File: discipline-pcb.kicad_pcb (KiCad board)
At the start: 2 copper layers, 304.9 x 122.8 mm, 180 parts, among them J1 AVR-ISP-6, SW1 KEYSW, SW10 KEYSW, SW11 KEYSW, SW12 KEYSW, SW13 KEYSW, SW14 KEYSW, SW15 KEYSW, SW16 KEYSW, SW17 KEYSW, SW18 KEYSW, SW19 KEYSW, SW2 KEYSW, SW20 KEYSW, SW21 KEYSW, SW22 KEYSW, SW23 KEYSW, SW24 KEYSW, SW25 KEYSW, SW26 KEYSW, SW27 KEYSW, SW28 KEYSW, SW29 KEYSW, SW3 KEYSW, SW30 KEYSW, SW31 KEYSW, SW32 KEYSW, SW33 KEYSW, SW34 KEYSW, SW35 KEYSW, SW36 KEYSW, SW37 KEYSW, SW38 KEYSW, SW39 KEYSW, SW4 KEYSW, SW40 KEYSW, SW41 KEYSW, SW42 KEYSW, SW43 KEYSW, SW44 KEYSW, SW45 KEYSW, SW46 KEYSW, SW47 KEYSW, SW48 KEYSW, SW49 KEYSW, SW5 KEYSW, SW50 KEYSW, SW51 KEYSW, SW52 KEYSW, SW53 KEYSW, SW54 KEYSW, SW55 KEYSW, SW56 KEYSW, SW57 KEYSW, SW58 KEYSW, SW59 KEYSW, SW6 KEYSW, SW60 KEYSW, SW61 KEYSW, SW62 KEYSW, SW63 KEYSW, SW64 KEYSW, SW65 KEYSW, SW66 KEYSW, SW67 KEYSW, SW68 KEYSW, SW7 KEYSW, SW8 KEYSW, SW9 KEYSW, U1 ATmega32A-PU, Y1 Crystal

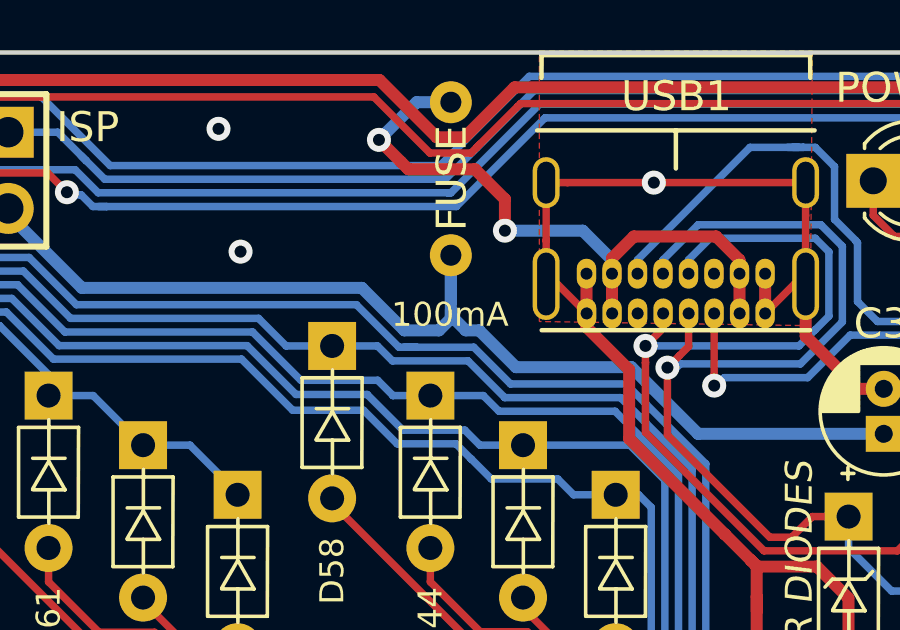
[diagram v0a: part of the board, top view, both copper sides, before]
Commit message: change fuse value
change fuse value from 100mA to 500mA. 100mA is fine for this use, but 500mA is USB 2.0 standard
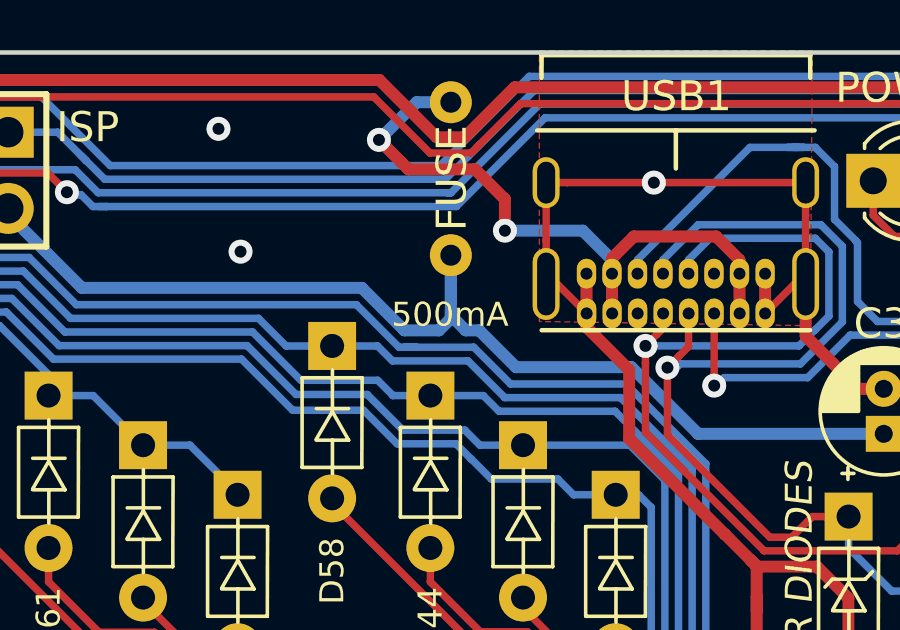
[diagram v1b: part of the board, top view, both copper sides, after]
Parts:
- F1: value 100mA -> 500mA
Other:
- board text added: "500mA"
- board text removed: "100mA"
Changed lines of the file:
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@@
       (effects (font (size 1 1) (thickness 0.15)))
     )
-    (fp_text value 100mA (at 0 -1.905 90) (layer F.Fab)
+    (fp_text value 500mA (at 0 -1.905 90) (layer F.Fab)
       (effects (font (size 1 1) (thickness 0.15)))
     )
@@
       (xy -5.108836 -0.98406)) (layer F.Cu) (width 0.01))
   )
-  (gr_text 100mA (at 276.795589 61.679275) (layer F.SilkS)
+  (gr_text 500mA (at 276.795589 61.679275) (layer F.SilkS)
     (effects (font (size 0.8 0.8) (thickness 0.1)))
   )

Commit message: Update discipline-pcb.kicad_pcb
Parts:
- removed ST62: 6.25U, MX_Alps_Hybrid:MX-6.25U-Stabilizer
- removed the SW31 at (75.0, 123.0)
- removed the SW59 at (77.4, 161.1)
- removed the SW61 at (106.0, 161.1)
- removed the SW62 at (187.0, 161.1)
- removed the SW63 at (268.0, 161.1)
- removed the SW64 at (296.5, 161.1)
- added REF**: 6.25U, cftkb:MX-6.25U-Stabilizer, F.Cu at (191.6, 166.2)
- added SW69: KEYSW, cftkb:SW_Cherry_MX1A_1.25u_PCBNOSCREEN, F.Cu at (75.0, 123.0)
- added SW70: KEYSW, cftkb:SW_Cherry_MX1A_1.50u_PCBNOSCREEN, F.Cu at (77.4, 161.1)
- added SW71: KEYSW, cftkb:SW_Cherry_MX1A_1.50u_PCBNOSCREEN, F.Cu at (106.0, 161.1)
- added SW72: KEYSW, cftkb:SW_Cherry_MX1A_1.00u_PCB-NOSCREEN, F.Cu at (187.0, 161.1)
- added SW73: KEYSW, cftkb:SW_Cherry_MX1A_1.50u_PCBNOSCREEN, F.Cu at (268.0, 161.1)
- added SW74: KEYSW, cftkb:SW_Cherry_MX1A_1.50u_PCBNOSCREEN, F.Cu at (296.5, 161.1)
- BOOT1, RESET1: footprint Button_Switch_THT:SW_PUSH_6mm -> cftkb:SW_PUSH_6mm
- C1, C2: footprint Capacitor_THT:C_Disc_D3.0mm_W1.6mm_P2.50mm -> cftkb:C_Disc_D3.0mm_W1.6mm_P2.50mm
- C3: footprint Capacitor_THT:CP_Radial_D4.0mm_P1.50mm -> cftkb:CP_Radial_D4.0mm_P1.50mm
- C4, C5: footprint Capacitor_THT:C_Disc_D4.3mm_W1.9mm_P5.00mm -> cftkb:C_Disc_D4.3mm_W1.9mm_P5.00mm
- D1, D10, D11, D12, D13, D14, D15, D16, D17, D18, D19, D2, D20, D21, D22, D23, D24, D25, D26, D27, D28, D29, D3, D30, D31, D32, D33, D34, D35, D36, D37, D38, D39, D4, D40, D41, D42, D43, D44, D45, D46, D47, D48, D49, D5, D50, D51, D52, D53, D54, D55, D56, D57, D58, D59, D6, D60, D61, D62, D63, D64, D65, D66, D67, D68, D7, D8, D9: footprint Diode_THT:D_DO-35_SOD27_P5.08mm_Horizontal -> cftkb:D_DO-35_SOD27_P5.08mm_Horizontal
- D69, D70: value 3V6 -> 3.6V; footprint Diode_THT:D_DO-35_SOD27_P5.08mm_Horizontal -> cftkb:D_DO-35_SOD27_P5.08mm_Horizontal
- F1: footprint keyboard_parts:polyfuse_5.1mm -> cftkb:polyfuse_5.1mm
- J1: footprint keyboard_parts:AVR_ICSP_3x2 -> cftkb:AVR_ICSP_3x2
- LED1: footprint LED_THT:LED_D3.0mm -> cftkb:LED_D3.0mm
- R1, R2, R3, R4, R6: footprint Resistor_THT:R_Axial_DIN0204_L3.6mm_D1.6mm_P7.62mm_Horizontal -> cftkb:R_Axial_DIN0204_L3.6mm_D1.6mm_P7.62mm_Horizontal
- R5: value 1.5K -> 1.5k; footprint Resistor_THT:R_Axial_DIN0204_L3.6mm_D1.6mm_P7.62mm_Horizontal -> cftkb:R_Axial_DIN0204_L3.6mm_D1.6mm_P7.62mm_Horizontal
- R7: value 10K -> 10k; footprint Resistor_THT:R_Axial_DIN0204_L3.6mm_D1.6mm_P7.62mm_Horizontal -> cftkb:R_Axial_DIN0204_L3.6mm_D1.6mm_P7.62mm_Horizontal
- ST72: renamed from ST62; footprint MX_Alps_Hybrid:MX-7U-Stabilizer -> cftkb:MX-7U-Stabilizer
- SW1, SW10, SW11, SW12, SW13, SW15, SW17, SW18, SW19, SW2, SW20, SW21, SW22, SW23, SW24, SW25, SW26, SW27, SW28, SW3, SW30, SW32, SW33, SW34, SW35, SW36, SW37, SW38, SW39, SW4, SW40, SW41, SW42, SW44, SW46, SW47, SW48, SW49, SW5, SW50, SW51, SW52, SW53, SW54, SW55, SW57, SW58, SW6, SW62, SW63, SW64, SW65, SW66, SW67, SW68, SW7, SW8, SW9: footprint Button_Switch_Keyboard:SW_Cherry_MX1A_1.00u_PCB-NOSCREEN -> cftkb:SW_Cherry_MX1A_1.00u_PCB-NOSCREEN
- SW14: footprint Button_Switch_Keyboard:SW_Cherry_MX1A_2.00u_PCBNOSCREEN -> cftkb:SW_Cherry_MX1A_2.00u_PCBNOSCREEN
- SW16, SW29: footprint Button_Switch_Keyboard:SW_Cherry_MX1A_1.50u_PCBNOSCREEN -> cftkb:SW_Cherry_MX1A_1.50u_PCBNOSCREEN
- SW31, SW56: footprint Button_Switch_Keyboard:SW_Cherry_MX1A_1.75u_PCBNOSCREEN -> cftkb:SW_Cherry_MX1A_1.75u_PCBNOSCREEN
- SW43, SW45: footprint Button_Switch_Keyboard:SW_Cherry_MX1A_2.25u_PCBNOSCREEN -> cftkb:SW_Cherry_MX1A_2.25u_PCBNOSCREEN
- SW59, SW60, SW61: footprint Button_Switch_Keyboard:SW_Cherry_MX1A_1.25u_PCBNOSCREEN -> cftkb:SW_Cherry_MX1A_1.25u_PCBNOSCREEN
- U1: footprint Package_DIP:DIP-40_W15.24mm -> cftkb:DIP-40_W15.24mm
- USB1: value USB_C_USB4085 -> USB_C_GCT_USB4085; footprint Type-C:USB_C_GCT_USB4085 -> cftkb:USB_C_GCT_USB4085
- Y1: footprint Crystal:Crystal_HC49-4H_Vertical -> cftkb:Crystal_HC49-4H_Vertical
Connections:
- net boot_led renamed Net-(U1-Pad15)
